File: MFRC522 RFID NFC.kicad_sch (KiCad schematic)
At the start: 25 parts, among them U1 MFRC522{slash}RC522

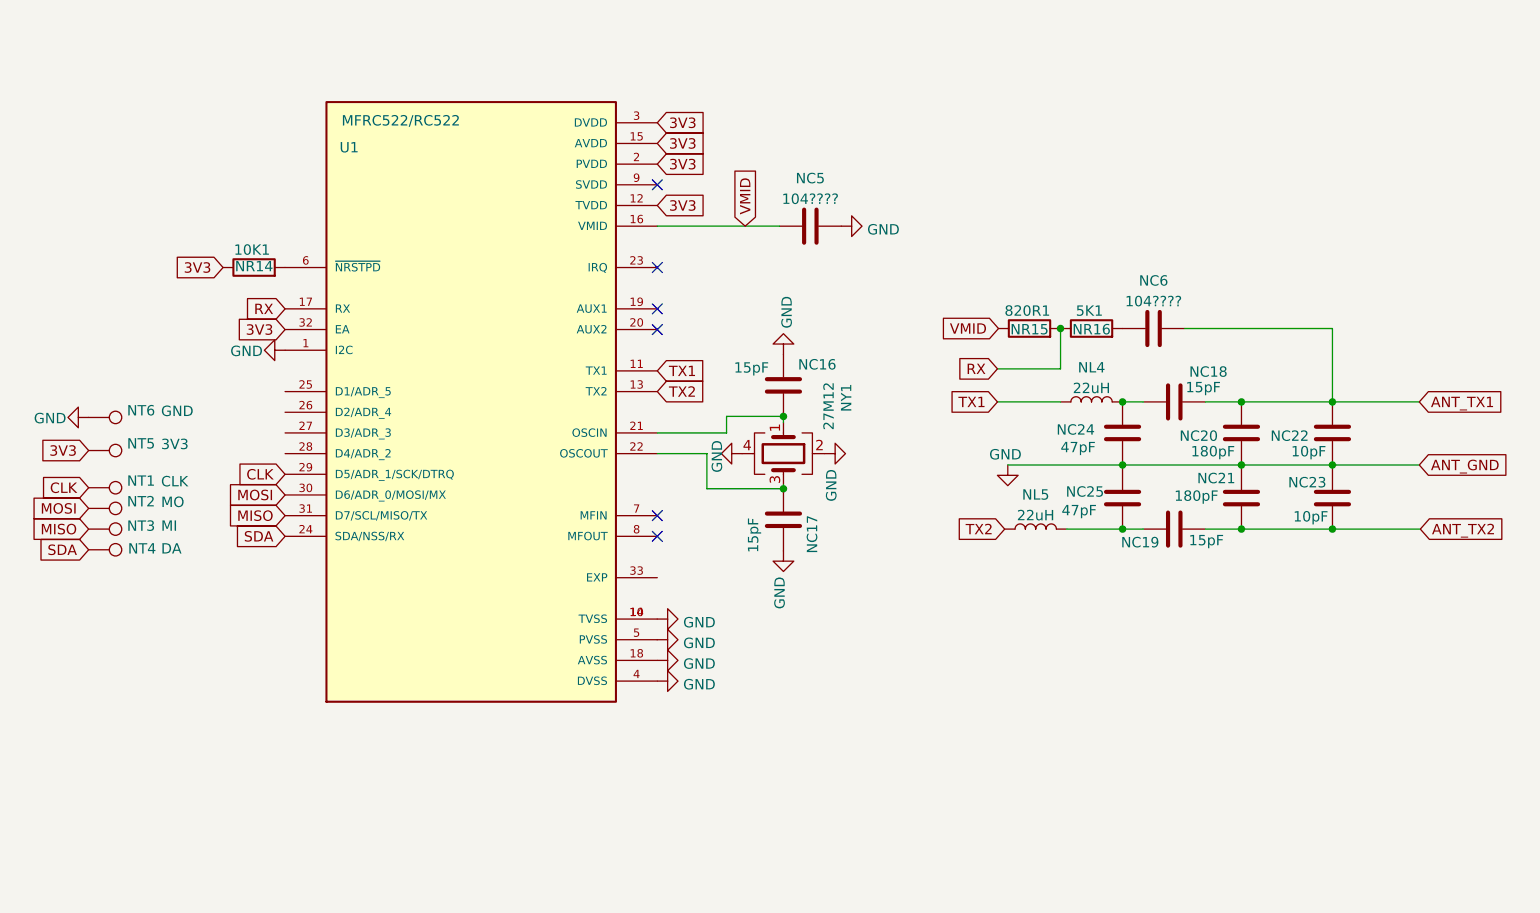
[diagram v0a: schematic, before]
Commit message: rev. 1.1
added missing components
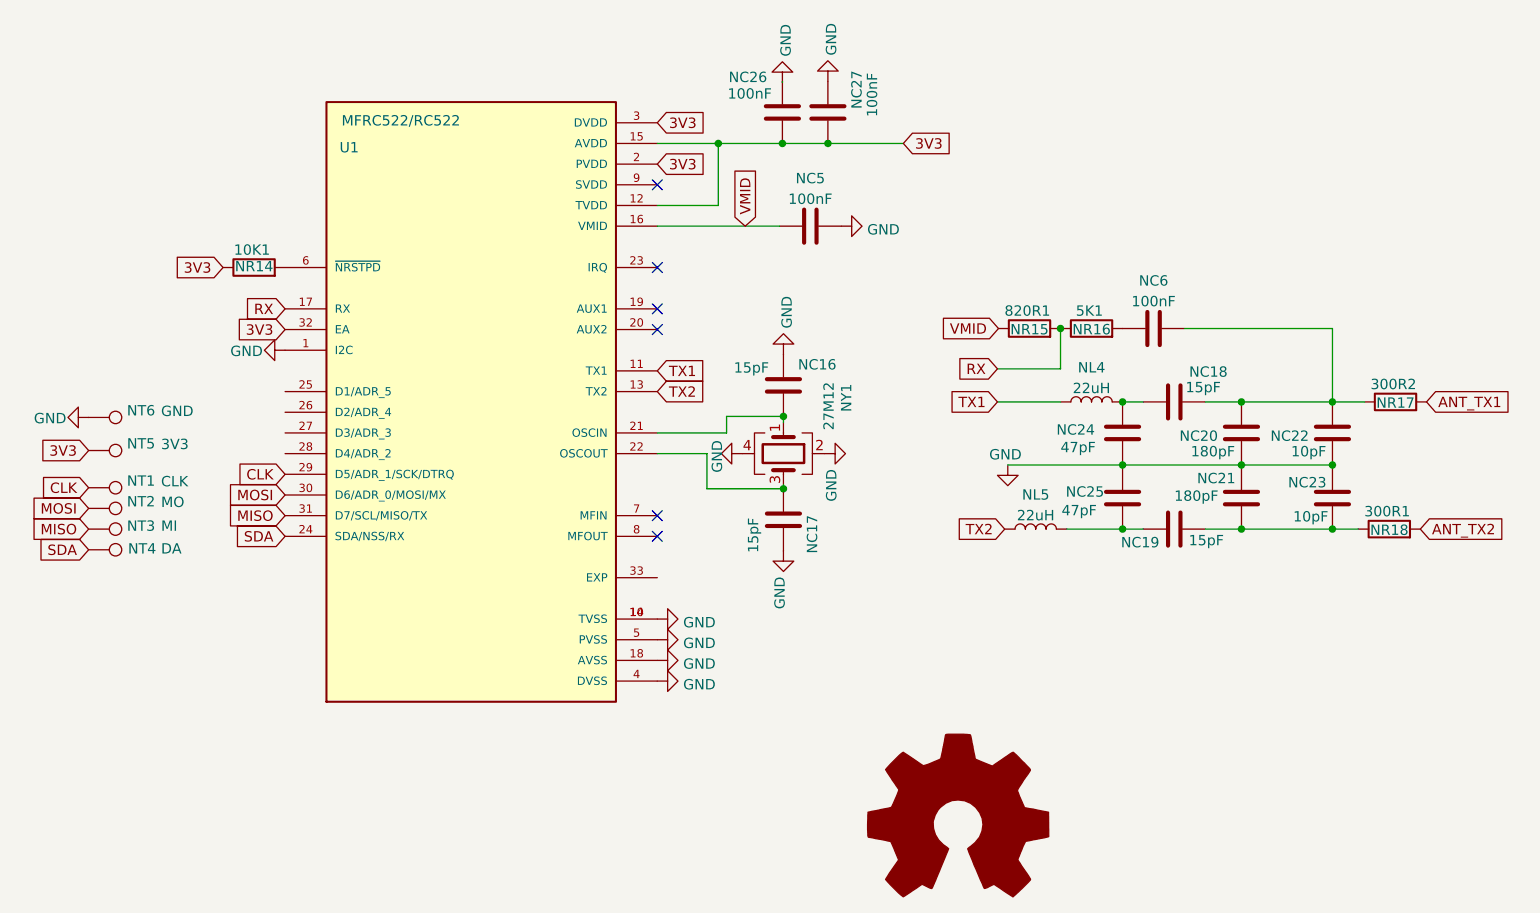
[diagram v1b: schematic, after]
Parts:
- added 300R1: NR18, Resistor_SMD:R_0805_2012Metric_Pad1.20x1.40mm_HandSolder, symbol Device:R
- added 300R2: NR17, Resistor_SMD:R_0805_2012Metric_Pad1.20x1.40mm_HandSolder, symbol Device:R
- added NC26, NC27: 100nF, Capacitor_SMD:C_0805_2012Metric_Pad1.18x1.45mm_HandSolder, symbol Device:C
- NC5, NC6: value 104???? -> 100nF
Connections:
- net 3V3: now also NC26.1, NC27.1
- net ANT_TX1: now also 300R2.2; no longer NC18.2, NC20.1, NC22.1, NC6.2
- net ANT_TX2: now also 300R1.2; no longer NC19.2, NC21.2, NC23.2
- net GND: now also NC26.2, NC27.2
- new net: 300R1.1, NC19.2, NC21.2, NC23.2
- new net: 300R2.1, NC18.2, NC20.1, NC22.1, NC6.2
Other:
- title: (none) -> Design by AeonLabs (www.aeonlabs.solutions)
